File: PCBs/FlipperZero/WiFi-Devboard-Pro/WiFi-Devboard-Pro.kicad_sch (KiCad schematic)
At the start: 30 parts

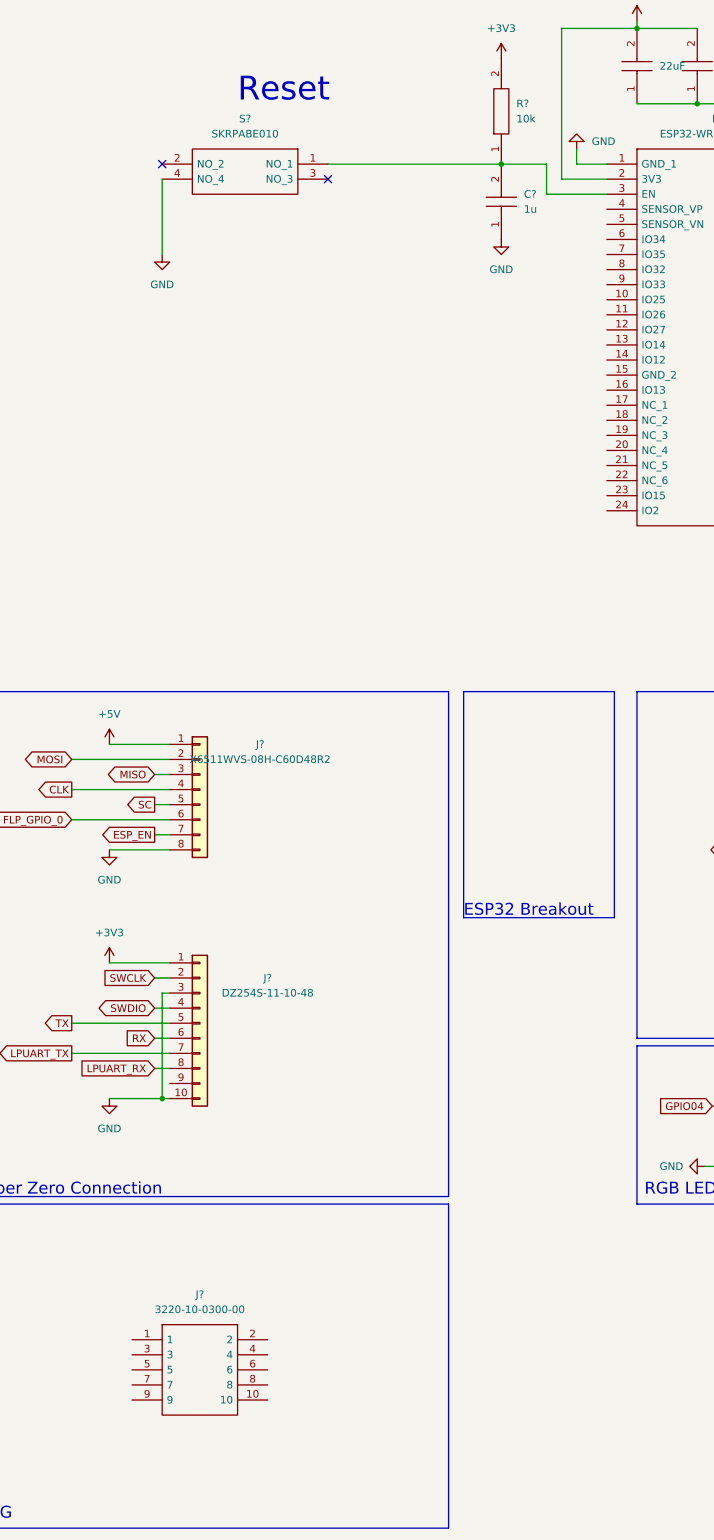
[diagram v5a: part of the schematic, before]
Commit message: Add wiring for JTAG
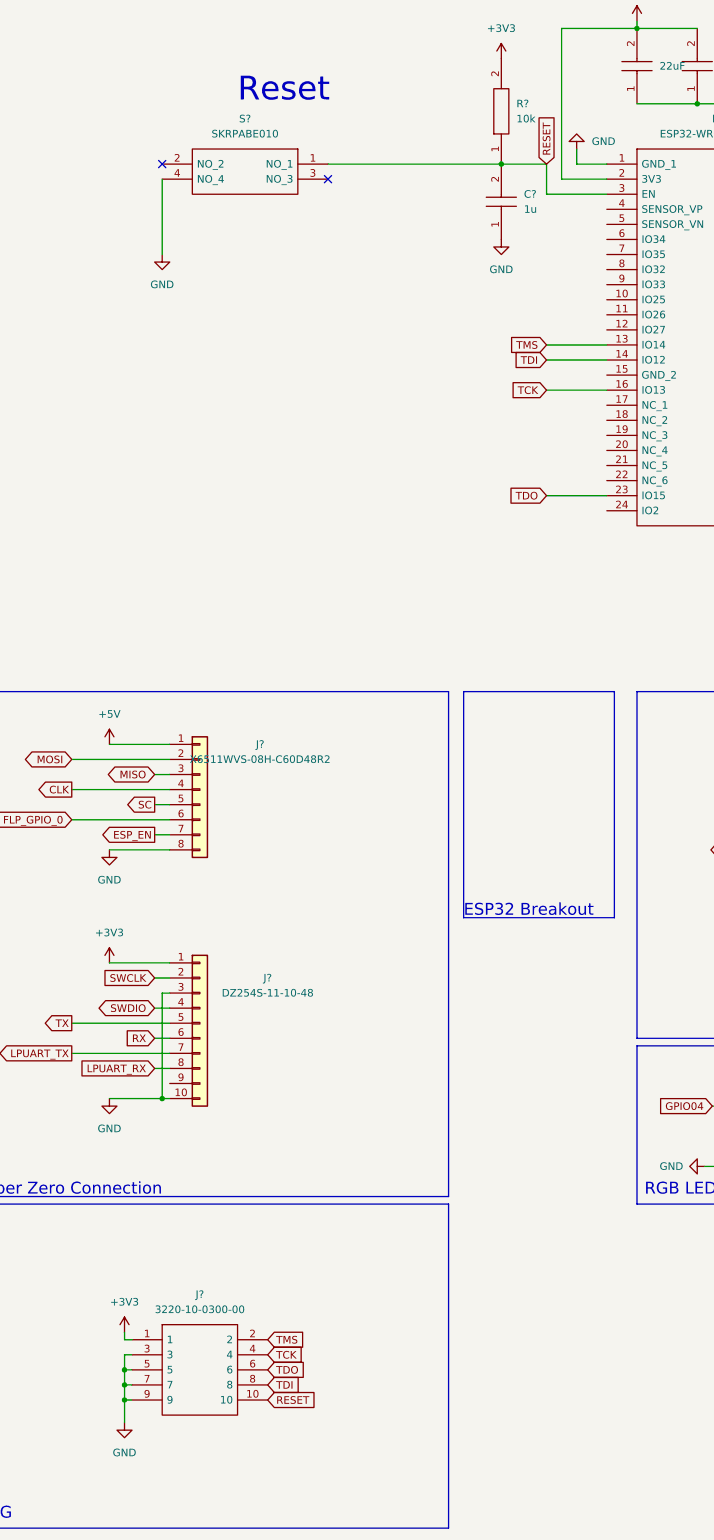
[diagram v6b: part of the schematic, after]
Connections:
- net +3V3: now also J?.1
- net GND: now also J?.3, J?.5, J?.7, J?.9
- net RESET: now reaches C?.2, IC?.3 (EN), R?.1, S?.1 (NO_1)
- net RESET: now also J?.10
- net TMS: now reaches IC?.13 (IO14)
- net TMS: now also J?.2
- net TDI: now reaches IC?.14 (IO12)
- net TDI: now also J?.8
- net TCK: now reaches IC?.16 (IO13)
- net TCK: now also J?.4
- net TDO: now reaches IC?.23 (IO15)
- net TDO: now also J?.6

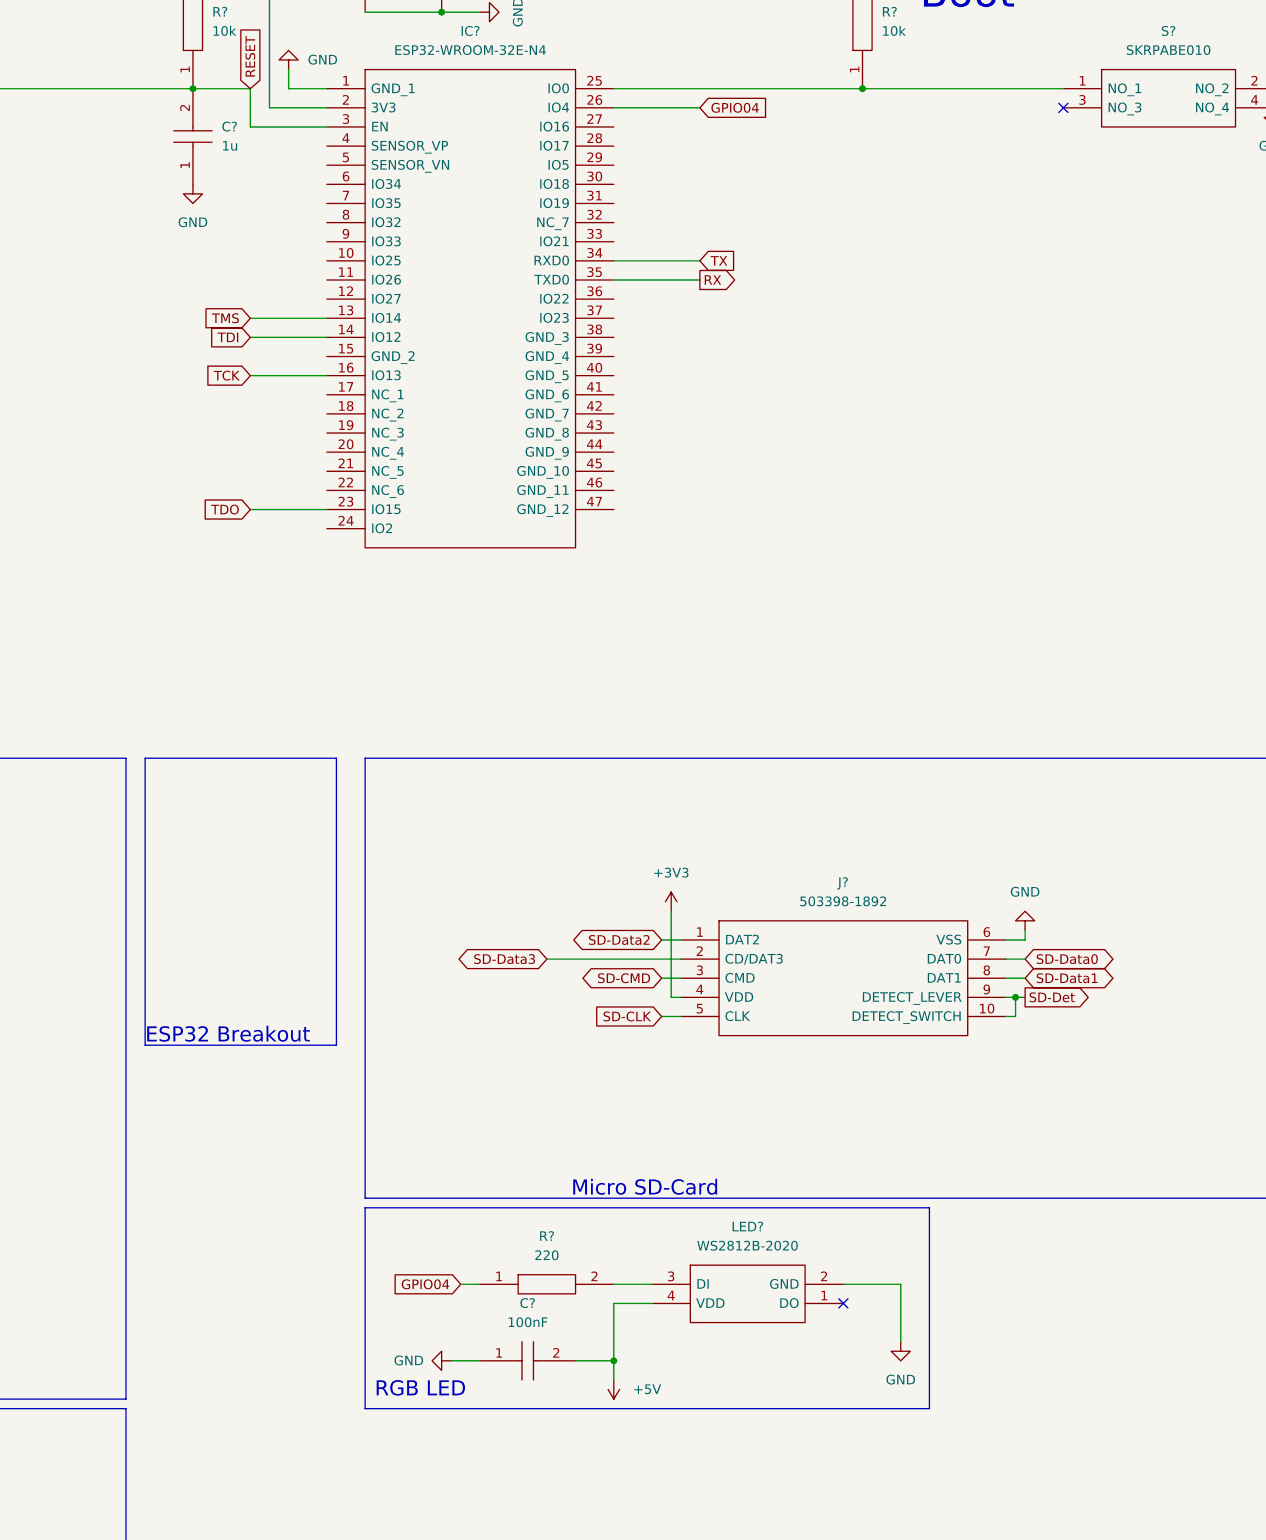
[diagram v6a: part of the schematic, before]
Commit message: Update SD connections
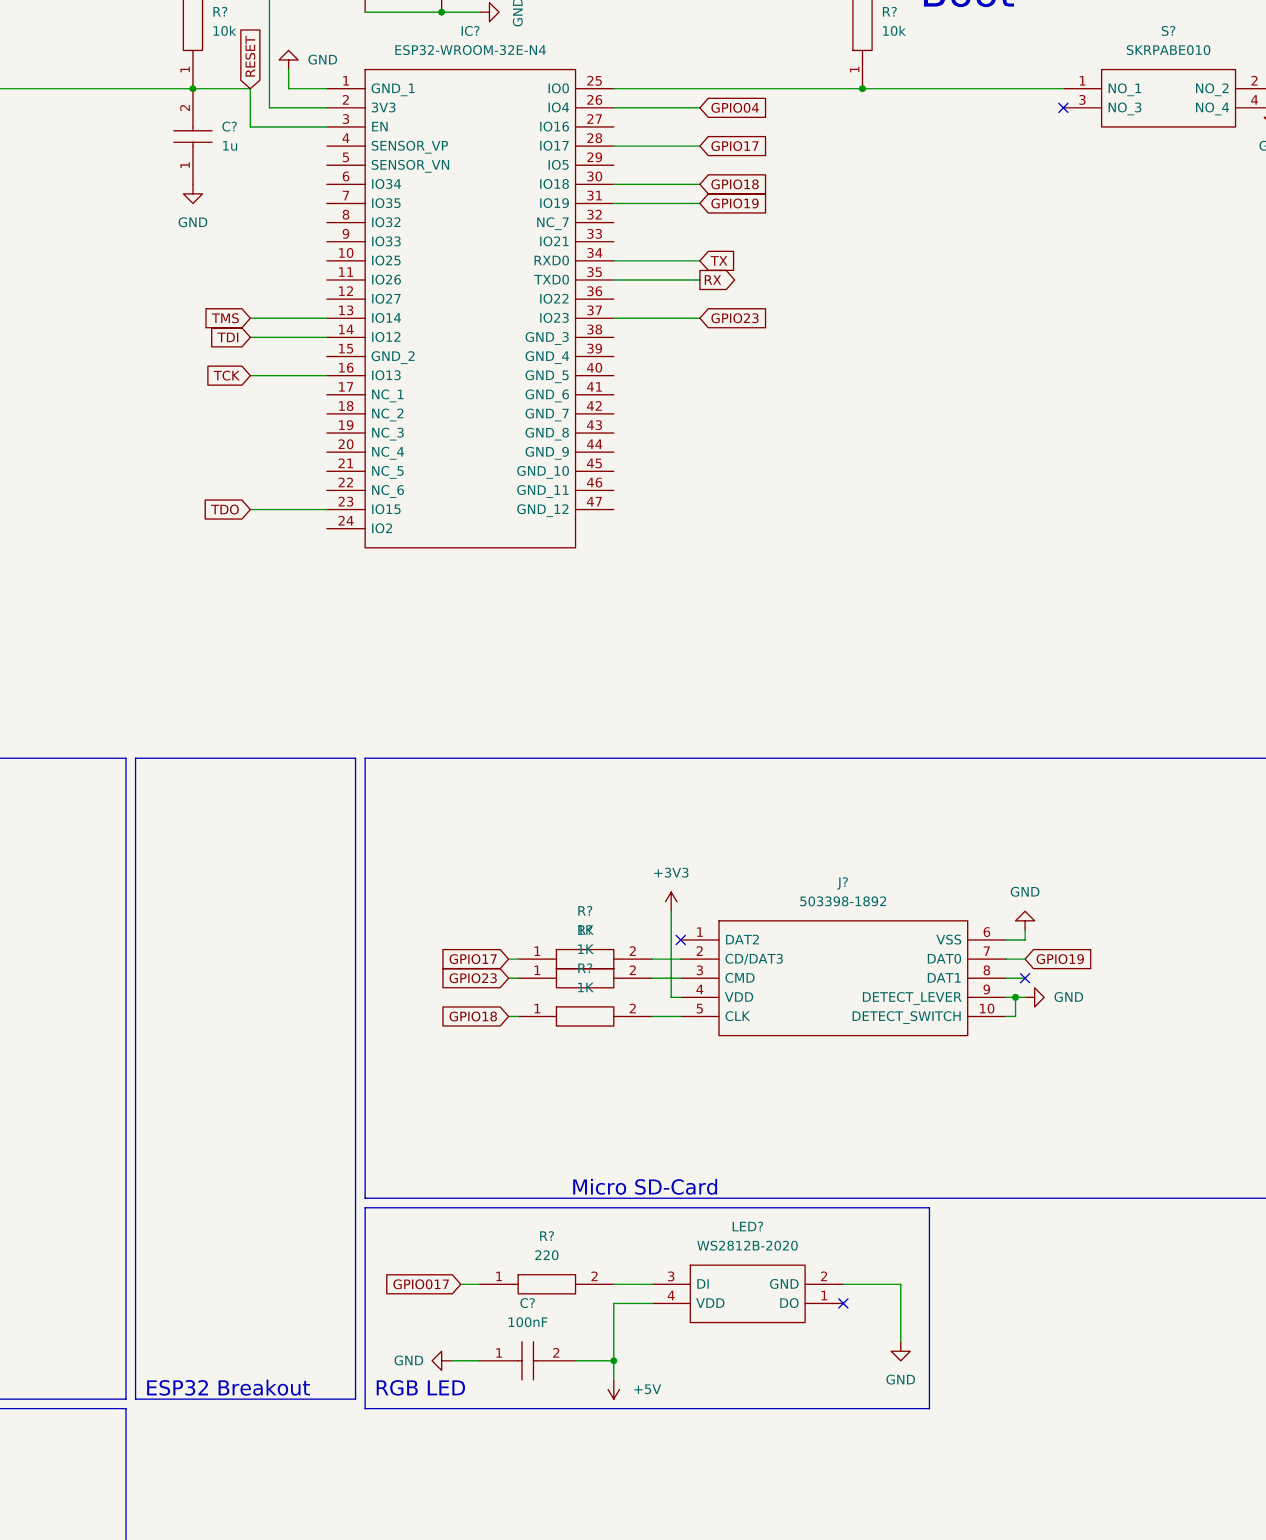
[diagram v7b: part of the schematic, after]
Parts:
- added R? (x3): 1K, RESC1005X40N, symbol SamacSys_Parts:RC0402FR-071KL
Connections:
- net SD-Data0 is gone; now on net GPIO19: J?.7 (DAT0)
- net SD-Det is gone; now on net GND: J?.10 (DETECT_SWITCH), J?.9 (DETECT_LEVER)
- net GPIO04: no longer R?.1
- net GPIO17: now reaches IC?.28 (IO17)
- net GPIO17: now also R?.1
- net GPIO18: now reaches IC?.30 (IO18)
- net GPIO18: now also R?.1
- net GPIO19: now reaches IC?.31 (IO19)
- net GPIO23: now reaches IC?.37 (IO23)
- net GPIO23: now also R?.1
- net SD-CLK: no longer names the net of J?.5 (CLK)
- net SD-CLK: now also R?.2
- net SD-CMD: no longer names the net of J?.3 (CMD)
- net SD-CMD: now also R?.2
- net SD-Data1: no longer names the net of J?.8 (DAT1)
- net SD-Data2: no longer names the net of J?.1 (DAT2)
- net SD-Data3: no longer names the net of J?.2 (CD/DAT3)
- net SD-Data3: now also R?.2
- new net GPIO017: R?.1
- no-connect marks 5 -> 7
